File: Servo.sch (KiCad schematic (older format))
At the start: 15 parts, among them P4 CONN_01X03, P5 CONN_01X03, P6 CONN_01X03, P7 CONN_01X03, U6 PCA9551

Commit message: Revisado V0.4. Actualizados gerber y esquemas
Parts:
- removed C10, C11, C8, C9: 1u, Capacitors_SMD:C_0805, symbol C
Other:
- note added: "Salidas a colector abierto"
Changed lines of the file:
@@
 Sheet 7 17
 Title "Puerto de expansión para servomotores"
-Date "2017-01-19"
+Date "2017-01-25"
 Rev "V.0.4"
 Comp "NanoPlayBoard"
@@
 	5250 3350 6350 3350
 Wire Wire Line
-	4250 1200 4250 1000
-$Comp
-L +5V #PWR029
-U 1 1 586D5A4A
-P 4250 1000
-F 0 "#PWR029" H 4250 850 50  0001 C CNN
-F 1 "+5V" H 4265 1173 50  0000 C CNN
-F 2 "" H 4250 1000 50  0000 C CNN
-F 3 "" H 4250 1000 50  0000 C CNN
-	1    4250 1000
-	1    0    0    -1
-$EndComp
-$Comp
-L +5V #PWR030
-U 1 1 586D5A77
-P 3900 1000
-F 0 "#PWR030" H 3900 850 50  0001 C CNN
-F 1 "+5V" H 3915 1173 50  0000 C CNN
-F 2 "" H 3900 1000 50  0000 C CNN
-F 3 "" H 3900 1000 50  0000 C CNN
-	1    3900 1000
-	1    0    0    -1
-$EndComp
-$Comp
-L +5V #PWR031
-U 1 1 586D5A9D
-P 3550 1000
-F 0 "#PWR031" H 3550 850 50  0001 C CNN
-F 1 "+5V" H 3565 1173 50  0000 C CNN
-F 2 "" H 3550 1000 50  0000 C CNN
-F 3 "" H 3550 1000 50  0000 C CNN
-	1    3550 1000
-	1    0    0    -1
-$EndComp
-$Comp
-L +5V #PWR032
-U 1 1 586D5AC3
-P 3200 1000
-F 0 "#PWR032" H 3200 850 50  0001 C CNN
-F 1 "+5V" H 3215 1173 50  0000 C CNN
-F 2 "" H 3200 1000 50  0000 C CNN
-F 3 "" H 3200 1000 50  0000 C CNN
-	1    3200 1000
-	1    0    0    -1
-$EndComp
-$Comp
-L GND #PWR033
-U 1 1 586D5AE2
-P 3200 1750
-F 0 "#PWR033" H 3200 1500 50  0001 C CNN
-F 1 "GND" H 3205 1577 50  0000 C CNN
-F 2 "" H 3200 1750 50  0000 C CNN
-F 3 "" H 3200 1750 50  0000 C CNN
-	1    3200 1750
-	1    0    0    -1
-$EndComp
-$Comp
-L GND #PWR034
-U 1 1 586D5B0F
-P 3550 1750
-F 0 "#PWR034" H 3550 1500 50  0001 C CNN
-F 1 "GND" H 3555 1577 50  0000 C CNN
-F 2 "" H 3550 1750 50  0000 C CNN
-F 3 "" H 3550 1750 50  0000 C CNN
-	1    3550 1750
-	1    0    0    -1
-$EndComp
-$Comp
-L GND #PWR035
-U 1 1 586D5B35
-P 3900 1750
-F 0 "#PWR035" H 3900 1500 50  0001 C CNN
-F 1 "GND" H 3905 1577 50  0000 C CNN
-F 2 "" H 3900 1750 50  0000 C CNN
-F 3 "" H 3900 1750 50  0000 C CNN
-	1    3900 1750
-	1    0    0    -1
-$EndComp
-$Comp
-L GND #PWR036
-U 1 1 586D5B5B
-P 4250 1750
-F 0 "#PWR036" H 4250 1500 50  0001 C CNN
-F 1 "GND" H 4255 1577 50  0000 C CNN
-F 2 "" H 4250 1750 50  0000 C CNN
-F 3 "" H 4250 1750 50  0000 C CNN
-	1    4250 1750
-	1    0    0    -1
-$EndComp
-Wire Wire Line
-	3200 1750 3200 1500
-Wire Wire Line
-	3200 1200 3200 1000
-Wire Wire Line
-	3550 1000 3550 1200
-Wire Wire Line
-	3900 1200 3900 1000
-Wire Wire Line
-	3900 1500 3900 1750
-Wire Wire Line
-	3550 1750 3550 1500
-Wire Wire Line
-	4250 1500 4250 1750
-Wire Wire Line
 	2450 1450 2450 2350
 $Comp
@@
 	1    0    0    -1
 $EndComp
-$Comp
-L C C8
-U 1 1 58701B7E
-P 3200 1350
-F 0 "C8" H 3315 1396 50  0000 L CNN
-F 1 "1u" H 3315 1305 50  0000 L CNN
-F 2 "Capacitors_SMD:C_0805" H 3238 1200 50  0001 C CNN
-F 3 "" H 3200 1350 50  0000 C CNN
-F 4 "SAMSUNG" H 3200 1350 60  0001 C CNN "Fabricante"
-F 5 "CL21B105KAFNNNE" H 3200 1350 60  0001 C CNN "Ref"
-F 6 "~" H 3200 1350 60  0001 C CNN "Potencia"
-F 7 "~" H 3200 1350 60  0001 C CNN "Tolerancia"
-F 8 "TME" H 3200 1350 60  0001 C CNN "Provedor"
-F 9 "CL21B105KAFNNNE" H 3200 1350 60  0001 C CNN "Ref_Proveedor"
-	1    3200 1350
-	1    0    0    -1
-$EndComp
-$Comp
-L C C9
-U 1 1 58701CA2
-P 3550 1350
-F 0 "C9" H 3665 1396 50  0000 L CNN
-F 1 "1u" H 3665 1305 50  0000 L CNN
-F 2 "Capacitors_SMD:C_0805" H 3588 1200 50  0001 C CNN
-F 3 "" H 3550 1350 50  0000 C CNN
-F 4 "SAMSUNG" H 3550 1350 60  0001 C CNN "Fabricante"
-F 5 "CL21B105KAFNNNE" H 3550 1350 60  0001 C CNN "Ref"
-F 6 "~" H 3550 1350 60  0001 C CNN "Potencia"
-F 7 "~" H 3550 1350 60  0001 C CNN "Tolerancia"
-F 8 "TME" H 3550 1350 60  0001 C CNN "Provedor"
-F 9 "CL21B105KAFNNNE" H 3550 1350 60  0001 C CNN "Ref_Proveedor"
-	1    3550 1350
-	1    0    0    -1
-$EndComp
-$Comp
-L C C10
-U 1 1 58701CFA
-P 3900 1350
-F 0 "C10" H 4015 1396 50  0000 L CNN
-F 1 "1u" H 4015 1305 50  0000 L CNN
-F 2 "Capacitors_SMD:C_0805" H 3938 1200 50  0001 C CNN
-F 3 "" H 3900 1350 50  0000 C CNN
-F 4 "SAMSUNG" H 3900 1350 60  0001 C CNN "Fabricante"
-F 5 "CL21B105KAFNNNE" H 3900 1350 60  0001 C CNN "Ref"
-F 6 "~" H 3900 1350 60  0001 C CNN "Potencia"
-F 7 "~" H 3900 1350 60  0001 C CNN "Tolerancia"
-F 8 "TME" H 3900 1350 60  0001 C CNN "Provedor"
-F 9 "CL21B105KAFNNNE" H 3900 1350 60  0001 C CNN "Ref_Proveedor"
-	1    3900 1350
-	1    0    0    -1
-$EndComp
-$Comp
-L C C11
-U 1 1 58701D4D
-P 4250 1350
-F 0 "C11" H 4365 1396 50  0000 L CNN
-F 1 "1u" H 4365 1305 50  0000 L CNN
-F 2 "Capacitors_SMD:C_0805" H 4288 1200 50  0001 C CNN
-F 3 "" H 4250 1350 50  0000 C CNN
-F 4 "SAMSUNG" H 4250 1350 60  0001 C CNN "Fabricante"
-F 5 "CL21B105KAFNNNE" H 4250 1350 60  0001 C CNN "Ref"
-F 6 "~" H 4250 1350 60  0001 C CNN "Potencia"
-F 7 "~" H 4250 1350 60  0001 C CNN "Tolerancia"
-F 8 "TME" H 4250 1350 60  0001 C CNN "Provedor"
-F 9 "CL21B105KAFNNNE" H 4250 1350 60  0001 C CNN "Ref_Proveedor"
-	1    4250 1350
-	1    0    0    -1
-$EndComp
 Wire Wire Line
 	2100 1450 2450 1450
@@
 ~RESET
 Connection ~ 1100 3050
+Text Notes 3000 2350 0    47   ~ 0
+Salidas a colector abierto
 $EndSCHEMATC

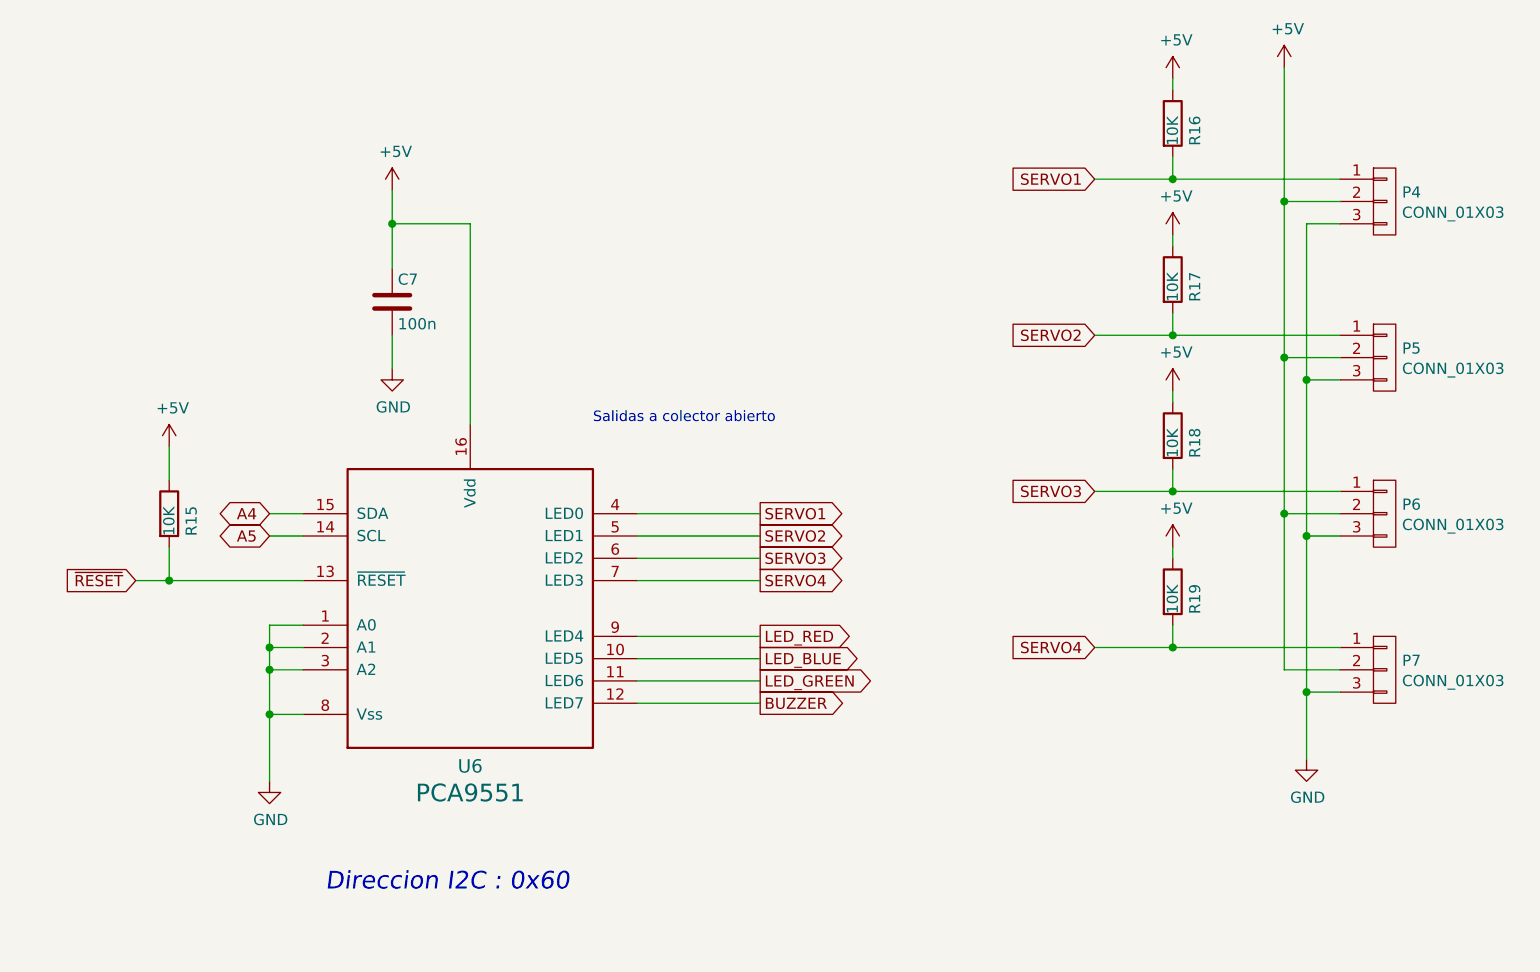
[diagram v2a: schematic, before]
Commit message: finalizada V0.4.1 corrige #17, #18 y #19
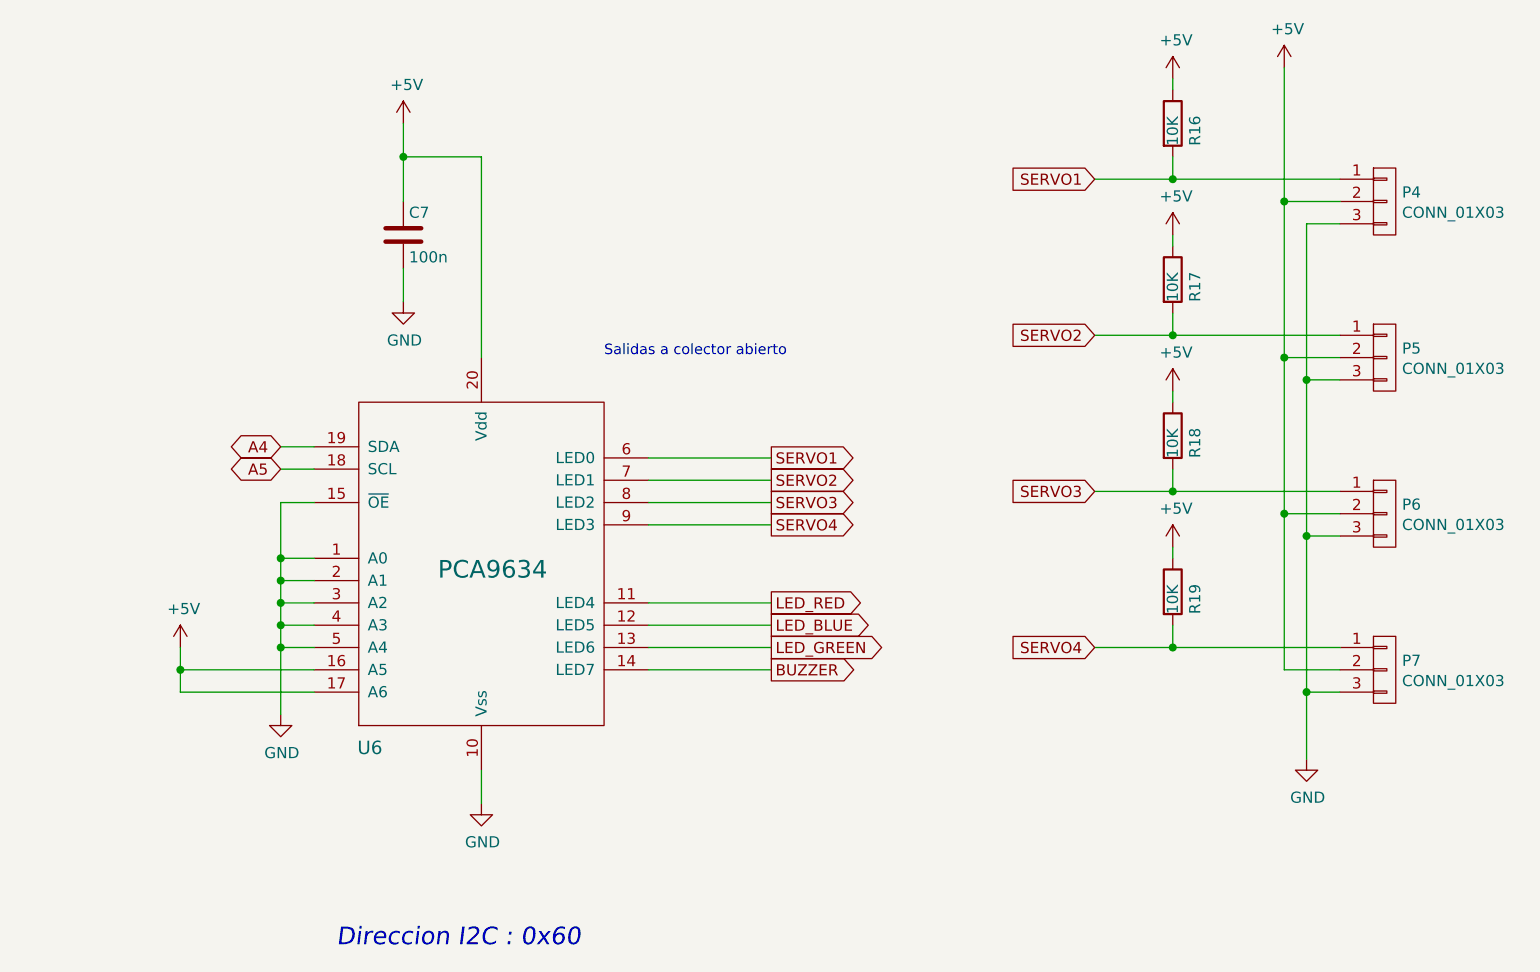
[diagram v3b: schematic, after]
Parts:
- removed R15: 10K, Resistencias:R_0805, symbol R
- removed U6: PCA9551, Housings_SSOP:TSSOP-16_4.4x5mm_Pitch0.65mm, symbol PCA9551
- added U6: PCA9634, Housings_SSOP:TSSOP-20_4.4x6.5mm_Pitch0.65mm, symbol PCA9634
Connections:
- net +5V: now also U6.16 (A5), U6.17 (A6), U6.20 (Vdd)
- net A4: now also U6.19 (SDA)
- net A5: now also U6.18 (SCL)
- net BUZZER: now also U6.14 (LED7)
- net GND: now also U6.1 (A0), U6.10 (Vss), U6.15 (~OE), U6.2 (A1), U6.3 (A2), U6.4 (A3), U6.5 (A4)
- net LED_BLUE: now also U6.12 (LED5)
- net LED_GREEN: now also U6.13 (LED6)
- net LED_RED: now also U6.11 (LED4)
- net SERVO1: now also U6.6 (LED0)
- net SERVO2: now also U6.7 (LED1)
- net SERVO3: now also U6.8 (LED2)
- net SERVO4: now also U6.9 (LED3)
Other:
- moved on the sheet: C7
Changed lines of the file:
@@
 LIBS:Pasivos
 LIBS:Reles
+LIBS:Arduino
 LIBS:Nano_PB-cache
 EELAYER 26 0
@@
 $EndBitmap
 $Comp
-L PCA9551 U6
-U 1 1 586D5351
-P 1900 3800
-F 0 "U6" H 2450 3717 60  0000 C CNN
-F 1 "PCA9551" H 2450 3597 79  0000 C CNN
-F 2 "Housings_SSOP:TSSOP-16_4.4x5mm_Pitch0.65mm" H 1900 3930 60  0001 C CNN
-F 3 "" H 1900 3930 60  0001 C CNN
-F 4 "510-730" H 2650 3600 60  0001 C CNN "Ref_Proveedor"
-F 5 "nxp" H 2300 3700 60  0001 C CNN "Fabricante"
-F 6 "PCA9551PW" H 2700 3700 60  0001 C CNN "Ref"
-F 7 "rs" H 2350 3600 60  0001 C CNN "Provedor"
-F 8 "" H 1900 3800 60  0001 C CNN "Tolerancia"
-F 9 "" H 1900 3800 60  0001 C CNN "Potencia"
-	1    1900 3800
-	1    0    0    -1
-$EndComp
-$Comp
 L CONN_01X03 P6
 U 1 1 586D53FE
@@
 	5250 3350 6350 3350
 Wire Wire Line
-	2450 1450 2450 2350
+	2500 1150 2500 2050
 $Comp
 L GND #PWR029
 U 1 1 586D5DFC
-P 2100 2100
-F 0 "#PWR029" H 2100 1850 50  0001 C CNN
-F 1 "GND" H 2105 1927 50  0000 C CNN
-F 2 "" H 2100 2100 50  0000 C CNN
-F 3 "" H 2100 2100 50  0000 C CNN
-	1    2100 2100
+P 2150 1800
+F 0 "#PWR029" H 2150 1550 50  0001 C CNN
+F 1 "GND" H 2155 1627 50  0000 C CNN
+F 2 "" H 2150 1800 50  0000 C CNN
+F 3 "" H 2150 1800 50  0000 C CNN
+	1    2150 1800
 	1    0    0    -1
 $EndComp
 Wire Wire Line
-	2100 2100 2100 1950
-Wire Wire Line
-	3200 2750 3750 2750
-Wire Wire Line
-	3200 2850 3750 2850
-Wire Wire Line
-	3200 2950 3750 2950
-Wire Wire Line
-	3200 3050 3750 3050
-Wire Wire Line
-	3200 3300 3750 3300
-Wire Wire Line
-	3200 3400 3750 3400
-Wire Wire Line
-	3200 3500 3750 3500
-Wire Wire Line
-	3200 3600 3750 3600
-Wire Wire Line
-	1550 3650 1700 3650
-Wire Wire Line
-	1550 3250 1550 3950
+	2150 1800 2150 1650
+Wire Wire Line
+	3250 2500 3800 2500
+Wire Wire Line
+	3250 2600 3800 2600
+Wire Wire Line
+	3250 2700 3800 2700
+Wire Wire Line
+	3250 2800 3800 2800
+Wire Wire Line
+	3250 3150 3800 3150
+Wire Wire Line
+	3250 3250 3800 3250
+Wire Wire Line
+	3250 3350 3800 3350
+Wire Wire Line
+	3250 3450 3800 3450
+Wire Wire Line
+	1600 3350 1750 3350
+Wire Wire Line
+	1600 2700 1600 3650
 $Comp
 L GND #PWR030
 U 1 1 586D660B
-P 1550 3950
-F 0 "#PWR030" H 1550 3700 50  0001 C CNN
-F 1 "GND" H 1555 3777 50  0000 C CNN
-F 2 "" H 1550 3950 50  0000 C CNN
-F 3 "" H 1550 3950 50  0000 C CNN
-	1    1550 3950
+P 1600 3650
+F 0 "#PWR030" H 1600 3400 50  0001 C CNN
+F 1 "GND" H 1605 3477 50  0000 C CNN
+F 2 "" H 1600 3650 50  0000 C CNN
+F 3 "" H 1600 3650 50  0000 C CNN
+	1    1600 3650
 	1    0    0    -1
 $EndComp
 Wire Wire Line
-	1700 3250 1550 3250
-Connection ~ 1550 3650
-Wire Wire Line
-	1550 3350 1700 3350
-Connection ~ 1550 3350
-Wire Wire Line
-	1700 3450 1550 3450
-Connection ~ 1550 3450
-Wire Wire Line
-	1700 2750 1550 2750
-Text GLabel 1550 2750 0    50   BiDi ~ 0
+	1750 2950 1600 2950
+Connection ~ 1600 3350
+Wire Wire Line
+	1600 3050 1750 3050
+Connection ~ 1600 3050
+Wire Wire Line
+	1750 3150 1600 3150
+Connection ~ 1600 3150
+Wire Wire Line
+	1750 2450 1600 2450
+Text GLabel 1600 2450 0    50   BiDi ~ 0
 A4
 Wire Wire Line
-	1550 2850 1700 2850
-Text GLabel 1550 2850 0    50   BiDi ~ 0
+	1600 2550 1750 2550
+Text GLabel 1600 2550 0    50   BiDi ~ 0
 A5
-Text GLabel 3750 3300 2    50   Output ~ 0
+Text GLabel 3800 3150 2    50   Output ~ 0
 LED_RED
-Text GLabel 3750 3500 2    50   Output ~ 0
+Text GLabel 3800 3350 2    50   Output ~ 0
 LED_GREEN
-Text GLabel 3750 3400 2    50   Output ~ 0
+Text GLabel 3800 3250 2    50   Output ~ 0
 LED_BLUE
-Text GLabel 3750 3600 2    50   Output ~ 0
+Text GLabel 3800 3450 2    50   Output ~ 0
 BUZZER
-Text GLabel 3750 2750 2    50   Output ~ 0
+Text GLabel 3800 2500 2    50   Output ~ 0
 SERVO1
-Text GLabel 3750 2850 2    50   Output ~ 0
+Text GLabel 3800 2600 2    50   Output ~ 0
 SERVO2
-Text GLabel 3750 2950 2    50   Output ~ 0
+Text GLabel 3800 2700 2    50   Output ~ 0
 SERVO3
-Text GLabel 3750 3050 2    50   Output ~ 0
+Text GLabel 3800 2800 2    50   Output ~ 0
 SERVO4
 Text GLabel 5250 1250 0    50   Input ~ 0
@@
 L +5V #PWR031
 U 1 1 586D839D
-P 2100 1300
-F 0 "#PWR031" H 2100 1150 50  0001 C CNN
-F 1 "+5V" H 2115 1473 50  0000 C CNN
-F 2 "" H 2100 1300 50  0000 C CNN
-F 3 "" H 2100 1300 50  0000 C CNN
-	1    2100 1300
+P 2150 1000
+F 0 "#PWR031" H 2150 850 50  0001 C CNN
+F 1 "+5V" H 2165 1173 50  0000 C CNN
+F 2 "" H 2150 1000 50  0000 C CNN
+F 3 "" H 2150 1000 50  0000 C CNN
+	1    2150 1000
 	1    0    0    -1
 $EndComp
 Wire Wire Line
-	2100 1300 2100 1650
-Connection ~ 2100 1450
+	2150 1000 2150 1350
+Connection ~ 2150 1150
 Wire Wire Line
 	5600 3250 5600 3350
@@
 Wire Wire Line
 	5600 2250 5600 2200
-Wire Wire Line
-	1100 2900 1100 3050
-Wire Wire Line
-	950  3050 1700 3050
-$Comp
-L +5V #PWR036
-U 1 1 58700007
-P 1100 2450
-F 0 "#PWR036" H 1100 2300 50  0001 C CNN
-F 1 "+5V" H 1115 2623 50  0000 C CNN
-F 2 "" H 1100 2450 50  0000 C CNN
-F 3 "" H 1100 2450 50  0000 C CNN
-	1    1100 2450
-	1    0    0    -1
-$EndComp
-Wire Wire Line
-	1100 2450 1100 2600
-$Comp
-L R R15
-U 1 1 58700C10
-P 1100 2750
-F 0 "R15" V 1200 2650 50  0000 L CNN
-F 1 "10K" V 1100 2650 50  0000 L CNN
-F 2 "Resistencias:R_0805" V 1030 2750 50  0001 C CNN
-F 3 "" H 1100 2750 50  0000 C CNN
-F 4 "VISHAY" H 1100 2750 60  0001 C CNN "Fabricante"
-F 5 "CRCW080510K0FKEA" H 1100 2750 60  0001 C CNN "Ref"
-F 6 "1/8W" H 1100 2750 60  0001 C CNN "Potencia"
-F 7 "1%" H 1100 2750 60  0001 C CNN "Tolerancia"
-F 8 "TME" H 1100 2750 60  0001 C CNN "Provedor"
-F 9 "CRCW080510K0FKEA" H 1100 2750 60  0001 C CNN "Ref_Proveedor"
-	1    1100 2750
-	1    0    0    -1
-$EndComp
 $Comp
 L R R19
@@
 L C C7
 U 1 1 58701807
-P 2100 1800
-F 0 "C7" H 2125 1900 50  0000 L CNN
-F 1 "100n" H 2125 1700 50  0000 L CNN
-F 2 "Capacitors_SMD:C_0805" H 2138 1650 50  0001 C CNN
-F 3 "" H 2100 1800 50  0000 C CNN
-F 4 "SAMSUNG" H 2100 1800 60  0001 C CNN "Fabricante"
-F 5 "CL21B104KBCNNNC" H 2100 1800 60  0001 C CNN "Ref"
-F 6 "~" H 2100 1800 60  0001 C CNN "Potencia"
-F 7 "~" H 2100 1800 60  0001 C CNN "Tolerancia"
-F 8 "TME" H 2100 1800 60  0001 C CNN "Provedor"
-F 9 "CL21B104KBCNNNC" H 2100 1800 60  0001 C CNN "Ref_Proveedor"
-	1    2100 1800
+P 2150 1500
+F 0 "C7" H 2175 1600 50  0000 L CNN
+F 1 "100n" H 2175 1400 50  0000 L CNN
+F 2 "Capacitors_SMD:C_0805" H 2188 1350 50  0001 C CNN
+F 3 "" H 2150 1500 50  0000 C CNN
+F 4 "SAMSUNG" H 2150 1500 60  0001 C CNN "Fabricante"
+F 5 "CL21B104KBCNNNC" H 2150 1500 60  0001 C CNN "Ref"
+F 6 "~" H 2150 1500 60  0001 C CNN "Potencia"
+F 7 "~" H 2150 1500 60  0001 C CNN "Tolerancia"
+F 8 "TME" H 2150 1500 60  0001 C CNN "Provedor"
+F 9 "CL21B104KBCNNNC" H 2150 1500 60  0001 C CNN "Ref_Proveedor"
+	1    2150 1500
 	1    0    0    -1
 $EndComp
 Wire Wire Line
-	2100 1450 2450 1450
-Text Notes 1800 4450 0    79   Italic 0
+	2150 1150 2500 1150
+Text Notes 1850 4700 0    79   Italic 0
 Direccion I2C : 0x60
-Text GLabel 950  3050 0    50   Input ~ 0
-~RESET
-Connection ~ 1100 3050
-Text Notes 3000 2350 0    47   ~ 0
+Text Notes 3050 2050 0    47   ~ 0
 Salidas a colector abierto
+$Comp
+L PCA9634 U6
+U 1 1 58BCA6EE
+P 1950 3700
+F 0 "U6" H 2000 3600 60  0000 C CNN
+F 1 "PCA9634" H 2550 4400 79  0000 C CNN
+F 2 "Housings_SSOP:TSSOP-20_4.4x6.5mm_Pitch0.65mm" H -650 880 60  0001 C CNN
+F 3 "" H -650 880 60  0001 C CNN
+	1    1950 3700
+	1    0    0    -1
+$EndComp
+Wire Wire Line
+	1750 3250 1600 3250
+Connection ~ 1600 3250
+Wire Wire Line
+	1750 3550 1150 3550
+Wire Wire Line
+	1150 3550 1150 3350
+Wire Wire Line
+	1750 3450 1150 3450
+Connection ~ 1150 3450
+$Comp
+L +5V #PWR036
+U 1 1 58BCAC34
+P 1150 3350
+F 0 "#PWR036" H 1150 3200 50  0001 C CNN
+F 1 "+5V" H 1165 3523 50  0000 C CNN
+F 2 "" H 1150 3350 50  0000 C CNN
+F 3 "" H 1150 3350 50  0000 C CNN
+	1    1150 3350
+	1    0    0    -1
+$EndComp
+Wire Wire Line
+	1750 2700 1600 2700
+Connection ~ 1600 2950
+$Comp
+L GND #PWR037
+U 1 1 58BCADAC
+P 2500 4050
+F 0 "#PWR037" H 2500 3800 50  0001 C CNN
+F 1 "GND" H 2505 3877 50  0000 C CNN
+F 2 "" H 2500 4050 50  0000 C CNN
+F 3 "" H 2500 4050 50  0000 C CNN
+	1    2500 4050
+	1    0    0    -1
+$EndComp
+Wire Wire Line
+	2500 4050 2500 3900
 $EndSCHEMATC
